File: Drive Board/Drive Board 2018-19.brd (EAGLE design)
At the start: 379.8 x 115 mm, 75 parts, among them IC1 ACS758KCB, IC2 ACS758KCB, IC3 ACS758KCB, IC4 ACS758KCB, IC5 7812T, IC6 LM741P, K1 G5L, K2 G5L, K3 G5L

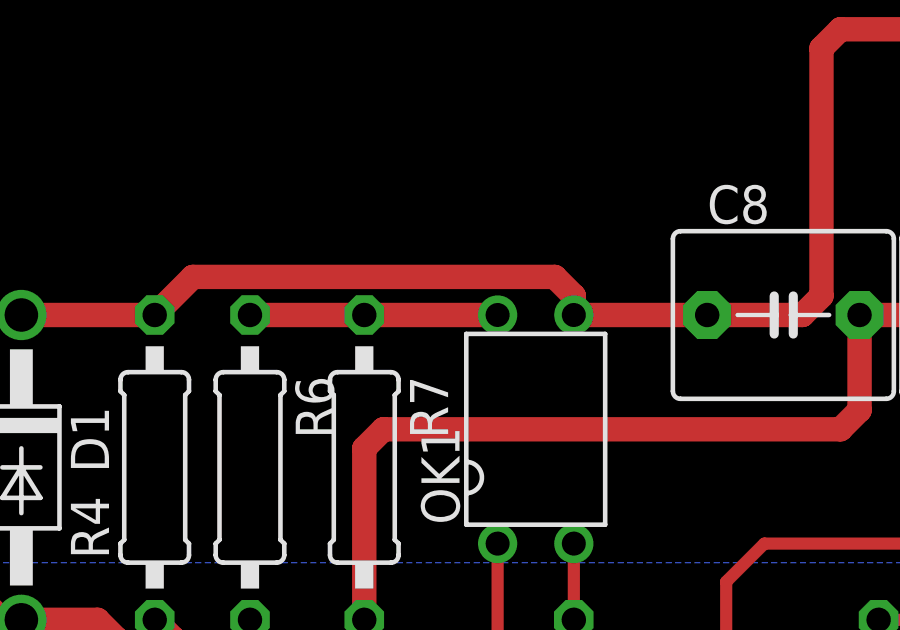
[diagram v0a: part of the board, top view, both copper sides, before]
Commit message: Fixed optocoupler mismatched pins
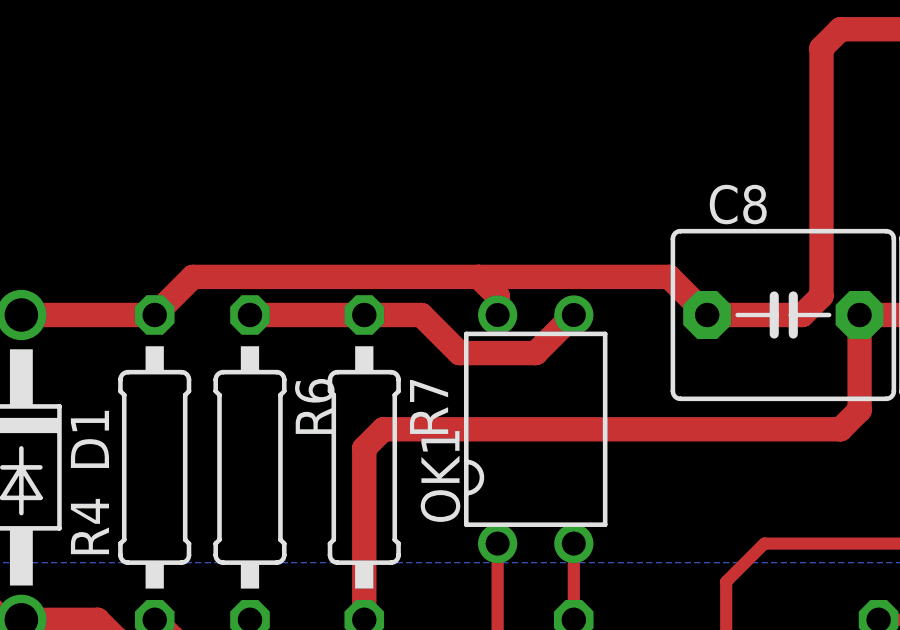
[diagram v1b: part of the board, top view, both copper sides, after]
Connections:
- net COIL_V+: now also OK1.4; no longer OK1.3
- net N$21: now also OK1.3; no longer OK1.4
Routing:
- net N$21: track 8.25 -> 11.8 mm
- net COIL_V+: track 217.7 -> 218.8 mm
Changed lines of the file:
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@@
 <contactref element="R6" pad="1"/>
 <contactref element="R7" pad="1"/>
-<contactref element="OK1" pad="4"/>
 <wire x1="140.335" y1="90.805" x2="136.525" y2="90.805" width="0.8128" layer="1"/>
-<wire x1="144.78" y1="90.805" x2="140.335" y2="90.805" width="0.8128" layer="1"/>
+<contactref element="OK1" pad="3"/>
+<wire x1="140.335" y1="90.805" x2="142.24" y2="90.805" width="0.8128" layer="1"/>
+<wire x1="142.24" y1="90.805" x2="143.51" y2="89.535" width="0.8128" layer="1"/>
+<wire x1="143.51" y1="89.535" x2="146.05" y2="89.535" width="0.8128" layer="1"/>
+<wire x1="146.05" y1="89.535" x2="147.32" y2="90.805" width="0.8128" layer="1"/>
 </signal>
 <signal name="N$29">
@@
 <contactref element="D1" pad="C"/>
 <contactref element="R4" pad="2"/>
-<contactref element="OK1" pad="3"/>
 <contactref element="U$11" pad="COI_V_+"/>
 <contactref element="K3" pad="2"/>
@@
 <wire x1="107.442" y1="91.694" x2="107.442" y2="90.043" width="0.8128" layer="1"/>
 <wire x1="107.442" y1="90.043" x2="107.95" y2="89.535" width="0.8128" layer="1"/>
-<wire x1="147.32" y1="90.805" x2="147.32" y2="91.44" width="0.8128" layer="1"/>
-<wire x1="147.32" y1="91.44" x2="146.685" y2="92.075" width="0.8128" layer="1"/>
-<wire x1="146.685" y1="92.075" x2="134.62" y2="92.075" width="0.8128" layer="1"/>
+<wire x1="144.145" y1="92.075" x2="134.62" y2="92.075" width="0.8128" layer="1"/>
 <wire x1="134.62" y1="92.075" x2="133.35" y2="90.805" width="0.8128" layer="1"/>
-<wire x1="147.32" y1="90.805" x2="151.765" y2="90.805" width="0.8128" layer="1"/>
 <wire x1="151.765" y1="90.805" x2="154.94" y2="90.805" width="0.8128" layer="1"/>
 <wire x1="154.94" y1="90.805" x2="155.575" y2="91.44" width="0.8128" layer="1"/>
@@
 <wire x1="18.415" y1="86.36" x2="15.24" y2="83.185" width="0.8128" layer="1"/>
 <wire x1="15.24" y1="83.185" x2="15.24" y2="46.99" width="0.8128" layer="1"/>
+<contactref element="OK1" pad="4"/>
+<wire x1="144.78" y1="90.805" x2="144.78" y2="91.44" width="0.8128" layer="1"/>
+<wire x1="144.78" y1="91.44" x2="144.145" y2="92.075" width="0.8128" layer="1"/>
+<wire x1="144.145" y1="92.075" x2="150.495" y2="92.075" width="0.8128" layer="1"/>
+<wire x1="150.495" y1="92.075" x2="151.765" y2="90.805" width="0.8128" layer="1"/>
 </signal>
 <signal name="OUT3">

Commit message: Update from chris meeting
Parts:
- removed S1: (no value), switch-dil:DS-01
- removed X4: (no value), con-molex-micro-fit-3_0:43045-0400
- added LED8: (no value), eagle-ltspice:LED_1206
- added R25: 100k, resistor:0207/10
- added R26: 500, resistor:0207/10
- added U$8: JTN1AS-PA-F-DC12V, RSX_driver_relay:JTN1AS-PA-F-DC12V
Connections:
- removed net N$29: B2.5V, S1.2
- removed net N$31: OK1.1, S1.1
- removed net N$33: B2.VIN, X4.P$4
- new net N$1: LED8.A, R26.1
- net 5V: now also B2.5V, R25.2; no longer X4.P$3
- net BATTERY_V+: now also U$8.VIN; no longer U$1.P$15, U$1.P$16, U$2.P$15, U$2.P$16, U$3.P$15, U$3.P$16, U$4.P$15, U$4.P$16, U$5.P$15, U$5.P$16, U$6.P$15, U$6.P$16
- net COIL_V+: now also B2.VIN, U$8.COI_V_+
- net COIL_V-: now also U$8.COIL_V_-
- net D12: now also OK1.1, R25.1, R26.2
- net GND: now also LED8.C; no longer X4.P$1, X4.P$2
- net N$24: now also U$8.NO
- net OUT2: now also U$13.P$10; no longer U$13.P$11
- net OUT4: now also U$1.P$15, U$1.P$16, U$2.P$15, U$2.P$16, U$3.P$15, U$3.P$16, U$4.P$15, U$4.P$16, U$5.P$15, U$5.P$16, U$6.P$15, U$6.P$16; no longer U$13.P$7
- net OUTA1: now also U$12.P$3; no longer U$12.P$1
- net OUTA3: now also U$12.P$1; no longer U$12.P$3
- net OUTA4: now also U$12.P$6; no longer U$12.P$4
- net OUTA6: now also U$12.P$4; no longer U$12.P$6
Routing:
- net D12: track 0.00 -> 143.2 mm
- net N$29: track 123.6 -> 0.00 mm
- net OUTA1: track 0.00 -> 118.2 mm
- net COIL_V+: track 218.8 -> 323.5 mm
- net OUTA6: track 0.00 -> 82.0 mm
- net OUTB1: track 0.00 -> 73.5 mm
- net OUTA2: track 0.00 -> 70.4 mm
- net OUTB6: track 0.00 -> 64.4 mm
- net IC3_IN: track 0.00 -> 59.4 mm
- net IC1_IN: track 0.00 -> 59.1 mm
- net GND: track 792.8 -> 734.9 mm, vias 1 -> 5
- net IC2_IN: track 0.00 -> 57.5 mm
- net OUTB2: track 0.00 -> 50.8 mm
- net OUTA5: track 0.00 -> 47.1 mm
- net OUTA4: track 0.00 -> 43.6 mm
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- added copper zone on layer 16, net OUT4
- removed copper zone on layer 16, net IC1_IN
- removed copper zone on layer 16, net IC2_IN
- removed copper zone on layer 16, net IC3_IN
- removed copper zone on layer 1, net OUT1
- removed copper zone on layer 1, net OUT2
- removed copper zone on layer 1, net OUT3
- removed copper zone on layer 1, net OUT4
- removed copper zone on layer 1, net OUTA1
- removed copper zone on layer 16, net OUTA2
- removed copper zone on layer 1, net OUTA3
- removed copper zone on layer 16, net OUTA4
- removed copper zone on layer 1, net OUTA5
- removed copper zone on layer 16, net OUTA6
- removed copper zone on layer 16, net OUTB1
- removed copper zone on layer 1, net OUTB2
- removed copper zone on layer 16, net OUTB3
- removed copper zone on layer 1, net OUTB4
- removed copper zone on layer 16, net OUTB5
- removed copper zone on layer 1, net OUTB6

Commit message: Added Larger GND Plane
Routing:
- net GND: track 734.9 -> 300.1 mm, vias 5 -> 4
- net 3V3: track 263.4 -> 269.2 mm

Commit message: Fixed Battery bay terminal pad connection
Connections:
- net BATTERY_V+: now also U$7.LEFTHOLE, U$7.P$2, U$7.RIGHTHOLE
- net GND: now also U$9.LEFTHOLE, U$9.P$2, U$9.RIGHTHOLE

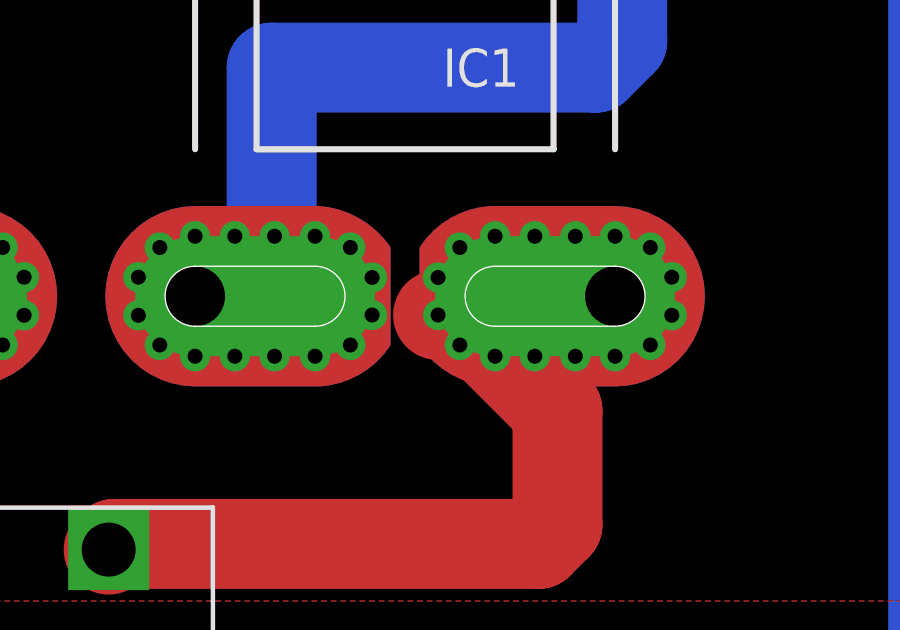
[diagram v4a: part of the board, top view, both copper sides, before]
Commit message: Fixed route size for planes
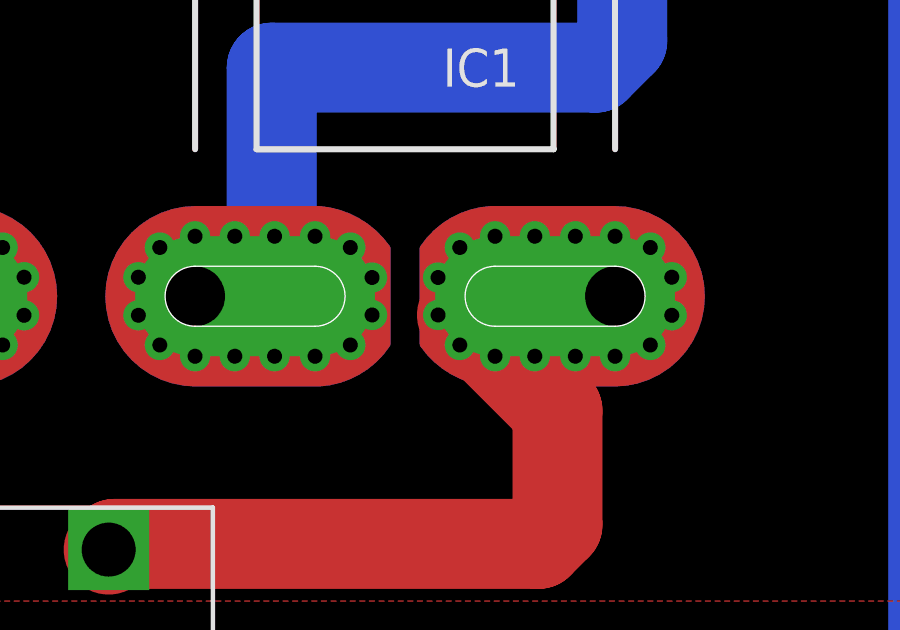
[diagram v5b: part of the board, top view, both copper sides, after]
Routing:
- net OUT1: track 24.4 -> 23.6 mm

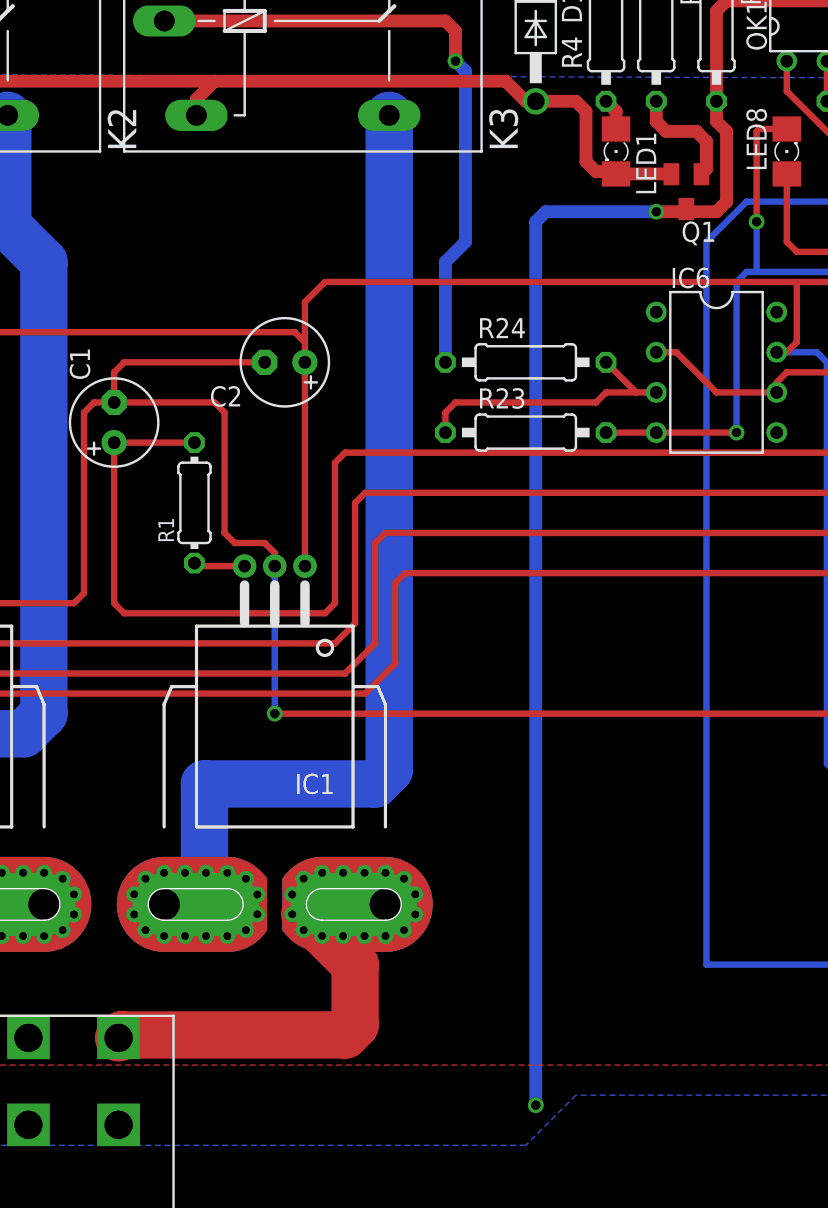
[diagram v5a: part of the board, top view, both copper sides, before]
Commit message: Fixed stray trace overlap
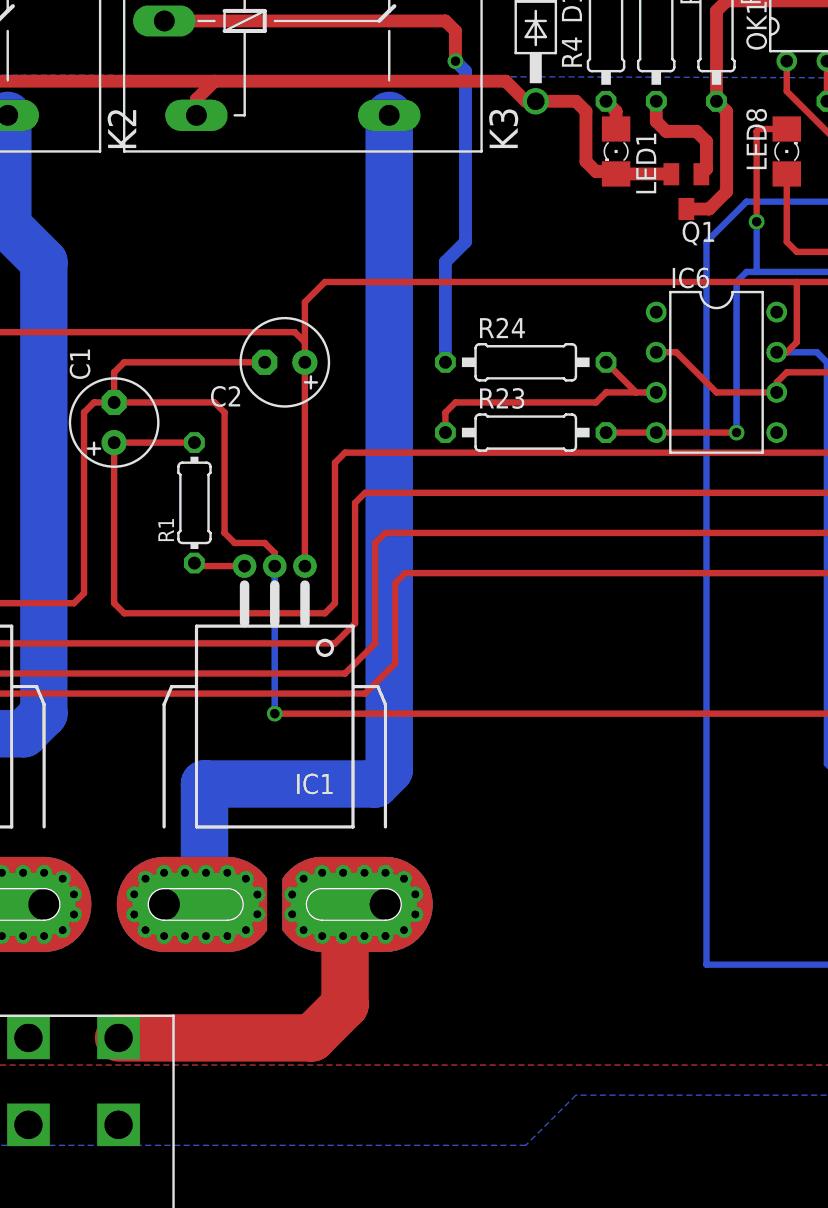
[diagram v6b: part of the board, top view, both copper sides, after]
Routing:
- net BATTERY_V-: track 122.1 -> 55.7 mm, vias 2 -> 0
- net OUT1: track 23.6 -> 19.6 mm
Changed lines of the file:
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@@
 <contactref element="IC1" pad="IP-@17" route="any" routetag="G$1.IP-"/>
 <contactref element="U$13" pad="P$12"/>
-<wire x1="114.29" y1="29.22" x2="117.475" y2="26.035" width="3" layer="1"/>
-<wire x1="117.475" y1="26.035" x2="117.475" y2="22.225" width="3" layer="1"/>
-<wire x1="117.475" y1="22.225" x2="116.84" y2="21.59" width="3" layer="1"/>
-<wire x1="116.84" y1="21.59" x2="102.705" y2="21.59" width="3" layer="1"/>
-<wire x1="102.705" y1="21.59" x2="102.515" y2="21.4" width="3" layer="1"/>
-<wire x1="114.29" y1="29.22" x2="113.495" y2="29.22" width="0" layer="19" extent="1-1"/>
+<wire x1="102.515" y1="21.4" x2="114.745" y2="21.4" width="3" layer="1"/>
+<wire x1="114.745" y1="21.4" x2="116.84" y2="23.495" width="3" layer="1"/>
+<wire x1="116.84" y1="23.495" x2="116.84" y2="27.725" width="3" layer="1"/>
+<wire x1="116.84" y1="27.725" x2="116.72" y2="27.845" width="3" layer="1"/>
 </signal>
 <signal name="N$52">
@@
 <contactref element="C7" pad="2"/>
 <contactref element="C8" pad="2"/>
-<wire x1="140.335" y1="80.645" x2="140.335" y2="79.375" width="0.8128" layer="1"/>
-<wire x1="140.335" y1="79.375" x2="140.97" y2="78.74" width="0.8128" layer="1"/>
-<wire x1="140.97" y1="78.74" x2="140.97" y2="74.295" width="0.8128" layer="1"/>
-<wire x1="140.97" y1="74.295" x2="140.335" y2="73.66" width="0.8128" layer="1"/>
-<wire x1="140.335" y1="73.66" x2="138.6" y2="73.66" width="0.8128" layer="1"/>
-<wire x1="138.6" y1="73.66" x2="138.43" y2="73.83" width="0.8128" layer="1"/>
 <wire x1="159.385" y1="90.805" x2="156.845" y2="90.805" width="0.8128" layer="1"/>
 <wire x1="156.845" y1="90.805" x2="156.845" y2="87.63" width="0.8128" layer="1"/>
@@
 <wire x1="166.37" y1="99.06" x2="167.005" y2="98.425" width="0.8128" layer="1"/>
 <wire x1="167.005" y1="95.885" x2="167.005" y2="98.425" width="0.8128" layer="1"/>
-<wire x1="138.6" y1="73.66" x2="136.525" y2="73.66" width="0.8128" layer="1"/>
-<via x="136.525" y="73.66" extent="1-16" drill="0.6" shape="square"/>
-<wire x1="136.525" y1="73.66" x2="129.54" y2="73.66" width="0.8128" layer="16"/>
-<wire x1="129.54" y1="73.66" x2="128.905" y2="73.025" width="0.8128" layer="16"/>
-<wire x1="128.905" y1="73.025" x2="128.905" y2="17.145" width="0.8128" layer="16"/>
-<via x="128.905" y="17.145" extent="1-16" drill="0.6" shape="square"/>
+<wire x1="138.43" y1="73.83" x2="139.87" y2="73.83" width="0.8128" layer="1"/>
+<wire x1="139.87" y1="73.83" x2="140.97" y2="74.93" width="0.8128" layer="1"/>
+<wire x1="140.97" y1="74.93" x2="140.97" y2="80.01" width="0.8128" layer="1"/>
+<wire x1="140.97" y1="80.01" x2="140.335" y2="80.645" width="0.8128" layer="1"/>
 </signal>
 <signal name="OUTA1">
